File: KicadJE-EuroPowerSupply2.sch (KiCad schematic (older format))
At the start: 48 parts, among them J101 Laptop Power, J102 +-15V thru, J103 +-12v out, J104 +5V out, J105 Laptop Power Out, J106 FrontInterConnVin, J107 BaseInterConnVin, J108 FrontInterConnVout, J109 BaseInterConnVout, P101 Doepfer_Power_10pin, P102 Doepfer_Power_16pin, P105 Doepfer_Power_10pin, P106 Doepfer_Power_16pin, SW101 SW_SPDT

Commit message: Init 750mA indicator
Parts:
- removed J108: FrontInterConnVout, AJ-Dropbox-Kicad:BoardConnector2x2.54x10mm4pin, symbol Connector:Conn_01x04_Male
- removed J109: BaseInterConnVout, AJ-Dropbox-Kicad:BoardConnector2x2.54x10mm4pin, symbol Connector:Conn_01x04_Male
- removed TP101, TP107: RED Sleeve, TestPoint:TestPoint_THTPad_D2.0mm_Drill1.0mm, symbol Connector:TestPoint
- removed TP102, TP108: RED Banana, MountingHole:MountingHole_6.4mm_M6_ISO14580_Pad, symbol Connector:TestPoint
- removed TP103: BLUE Sleeve, TestPoint:TestPoint_THTPad_D2.0mm_Drill1.0mm, symbol Connector:TestPoint
- removed TP104: BLUE Banana, MountingHole:MountingHole_6.4mm_M6_ISO14580_Pad, symbol Connector:TestPoint
- removed TP105: BLACK Sleeve, TestPoint:TestPoint_THTPad_D2.0mm_Drill1.0mm, symbol Connector:TestPoint
- removed TP106: BLACK Banana, MountingHole:MountingHole_6.4mm_M6_ISO14580_Pad, symbol Connector:TestPoint
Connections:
- wire segments 233 -> 213
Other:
- moved on the sheet: J106, J107

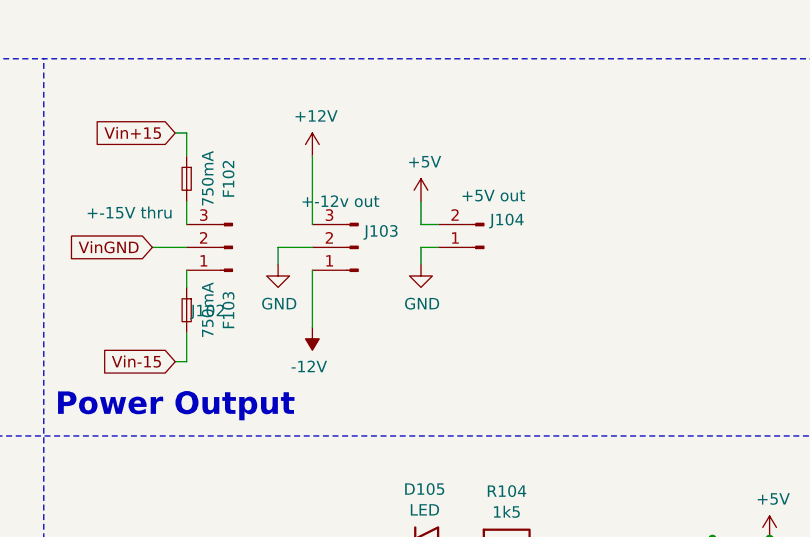
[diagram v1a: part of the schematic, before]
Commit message: placing first components
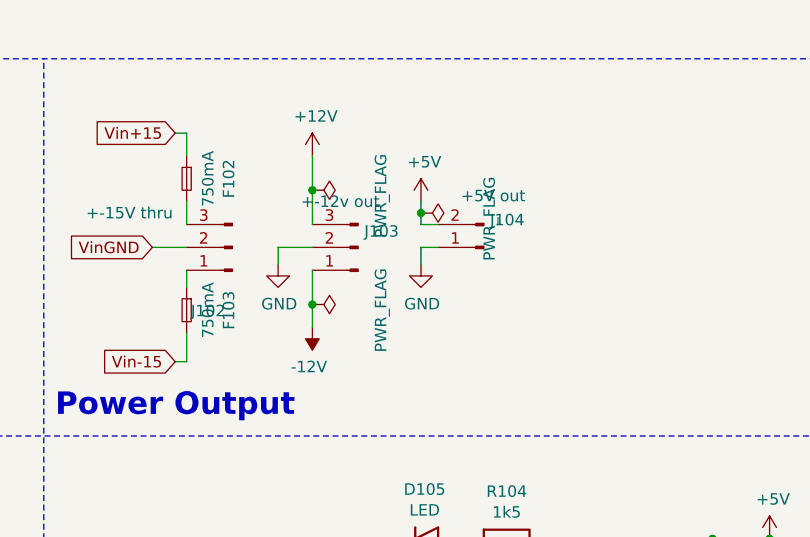
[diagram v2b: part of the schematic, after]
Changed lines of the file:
@@
 	5250 1800 5250 1925
 Wire Wire Line
-	5800 1025 5800 1325
-Wire Wire Line
-	5800 1775 5800 1525
+	5800 1025 5800 1175
+Wire Wire Line
+	5800 1775 5800 1675
 Wire Wire Line
 	4250 2625 4250 2825
@@
 	6350 1325 6275 1325
 Wire Wire Line
-	6275 1325 6275 1225
+	6275 1325 6275 1275
 $Comp
 L power:PWR_FLAG #FLG0101
@@
 Wire Notes Line
 	8350 3800 6000 3800
+$Comp
+L power:PWR_FLAG #FLG0104
+U 1 1 5F317544
+P 5800 1175
+AR Path="/5F317544" Ref="#FLG0104"  Part="1"
+AR Path="/5CBAA806/5F317544" Ref="#FLG?"  Part="1"
+F 0 "#FLG0104" H 5800 1250 50  0001 C CNN
+F 1 "PWR_FLAG" H 5825 1475 50  0000 C CNN
+F 2 "" H 5800 1175 50  0001 C CNN
+F 3 "~" H 5800 1175 50  0001 C CNN
+	1    5800 1175
+	0    1    1    0
+$EndComp
+Connection ~ 5800 1175
+Wire Wire Line
+	5800 1175 5800 1325
+$Comp
+L power:PWR_FLAG #FLG0105
+U 1 1 5F31A053
+P 5800 1675
+AR Path="/5F31A053" Ref="#FLG0105"  Part="1"
+AR Path="/5CBAA806/5F31A053" Ref="#FLG?"  Part="1"
+F 0 "#FLG0105" H 5800 1750 50  0001 C CNN
+F 1 "PWR_FLAG" H 5825 1975 50  0000 C CNN
+F 2 "" H 5800 1675 50  0001 C CNN
+F 3 "~" H 5800 1675 50  0001 C CNN
+	1    5800 1675
+	0    1    1    0
+$EndComp
+Connection ~ 5800 1675
+Wire Wire Line
+	5800 1675 5800 1525
+$Comp
+L power:PWR_FLAG #FLG0106
+U 1 1 5F31A50C
+P 6275 1275
+AR Path="/5F31A50C" Ref="#FLG0106"  Part="1"
+AR Path="/5CBAA806/5F31A50C" Ref="#FLG?"  Part="1"
+F 0 "#FLG0106" H 6275 1350 50  0001 C CNN
+F 1 "PWR_FLAG" H 6300 1575 50  0000 C CNN
+F 2 "" H 6275 1275 50  0001 C CNN
+F 3 "~" H 6275 1275 50  0001 C CNN
+	1    6275 1275
+	0    1    1    0
+$EndComp
+Connection ~ 6275 1275
+Wire Wire Line
+	6275 1275 6275 1225
 $EndSCHEMATC

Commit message: interboard connector
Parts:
- removed J107: BaseInterConnVin, AJ-Dropbox-Kicad:BoardConnector2x2.54x10mm4pin, symbol Connector:Conn_01x02_Male
- added J?: FrontInterConnVin, Connector_PinHeader_2.54mm:PinHeader_1x04_P2.54mm_Vertical, symbol Connector:Conn_01x04_Male
- added J? (x2): Conn_01x08, Connector_PinHeader_2.54mm:PinHeader_1x08_P2.54mm_Vertical, symbol Connector_Generic:Conn_01x08
- J106: footprint AJ-Dropbox-Kicad:BoardConnector2x2.54x10mm4pin -> Connector_PinHeader_2.54mm:PinHeader_1x04_P2.54mm_Vertical; symbol Connector:Conn_01x02_Male -> Connector:Conn_01x04_Male
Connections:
- net +12V: now also J?.5 (Pin_5), J?.5 (Pin_5)
- net +5V: now also J?.3 (Pin_3), J?.3 (Pin_3)
- net -12V: now also J?.7 (Pin_7), J?.7 (Pin_7)
- net GND: now also J?.1 (Pin_1), J?.1 (Pin_1), J?.8 (Pin_8), J?.8 (Pin_8)
- net Vin-Neg19: now also J106.3 (Pin_3), J106.4 (Pin_4), J?.3 (Pin_3), J?.4 (Pin_4); no longer J106.2 (Pin_2)
- net Vin-Pos19: now also J106.2 (Pin_2), J?.1 (Pin_1), J?.2 (Pin_2)
- new net I+12: J?.4 (Pin_4), J?.4 (Pin_4)
- new net I+5: J?.2 (Pin_2), J?.2 (Pin_2)
- new net I-12: J?.6 (Pin_6), J?.6 (Pin_6)
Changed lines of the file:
@@
 	6150 2900 7550 2900
 $Comp
-L Connector:Conn_01x02_Male J106
+L Connector:Conn_01x04_Male J106
 U 1 1 5C9B2CF1
 P 6275 4275
 F 0 "J106" H 6381 4453 50  0000 C CNN
 F 1 "FrontInterConnVin" H 6381 4362 50  0000 C CNN
-F 2 "AJ-Dropbox-Kicad:BoardConnector2x2.54x10mm4pin" H 6275 4275 50  0001 C CNN
+F 2 "Connector_PinHeader_2.54mm:PinHeader_1x04_P2.54mm_Vertical" H 6275 4275 50  0001 C CNN
 F 3 "~" H 6275 4275 50  0001 C CNN
 	1    6275 4275
 	1    0    0    -1
-$EndComp
-$Comp
-L Connector:Conn_01x02_Male J107
-U 1 1 5C9B2E76
-P 7425 4275
-F 0 "J107" H 7398 4248 50  0000 R CNN
-F 1 "BaseInterConnVin" H 7398 4157 50  0000 R CNN
-F 2 "AJ-Dropbox-Kicad:BoardConnector2x2.54x10mm4pin" H 7425 4275 50  0001 C CNN
-F 3 "~" H 7425 4275 50  0001 C CNN
-	1    7425 4275
-	-1   0    0    -1
 $EndComp
 Text GLabel 6975 4175 2    50   Input ~ 0
@@
 	6475 4375 6825 4375
 Wire Wire Line
-	7225 4275 6825 4275
-Wire Wire Line
 	6975 4475 6825 4475
 Wire Wire Line
 	6825 4475 6825 4375
 Connection ~ 6825 4375
-Wire Wire Line
-	6825 4375 7225 4375
 Wire Wire Line
 	6975 4175 6825 4175
@@
 Wire Wire Line
 	6275 1275 6275 1225
+Text GLabel 9150 4175 0    59   Input ~ 0
+I+5
+Wire Wire Line
+	9150 4175 9175 4175
+Text GLabel 9175 4575 0    59   Input ~ 0
+I-12
+Text GLabel 9175 4375 0    59   Input ~ 0
+I+12
+$Comp
+L Connector:Conn_01x04_Male J?
+U 1 1 5F5803FF
+P 7850 4275
+F 0 "J?" H 7956 4453 50  0000 C CNN
+F 1 "FrontInterConnVin" H 7956 4362 50  0000 C CNN
+F 2 "Connector_PinHeader_2.54mm:PinHeader_1x04_P2.54mm_Vertical" H 7850 4275 50  0001 C CNN
+F 3 "~" H 7850 4275 50  0001 C CNN
+	1    7850 4275
+	-1   0    0    -1
+$EndComp
+Wire Wire Line
+	7650 4175 7650 4275
+Wire Wire Line
+	6825 4275 7650 4275
+Connection ~ 7650 4275
+Wire Wire Line
+	7650 4475 7650 4375
+Wire Wire Line
+	6825 4375 7650 4375
+Connection ~ 7650 4375
+Wire Wire Line
+	6475 4475 6475 4375
+Connection ~ 6475 4375
+Wire Wire Line
+	6475 4275 6475 4175
+Connection ~ 6475 4275
+$Comp
+L power:-12V #PWR?
+U 1 1 5F5B2912
+P 9175 4675
+F 0 "#PWR?" H 9175 4775 50  0001 C CNN
+F 1 "-12V" H 9190 4848 50  0000 C CNN
+F 2 "" H 9175 4675 50  0001 C CNN
+F 3 "" H 9175 4675 50  0001 C CNN
+	1    9175 4675
+	0    -1   -1   0
+$EndComp
+$Comp
+L power:GND #PWR?
+U 1 1 5F5B2F3A
+P 9175 4775
+F 0 "#PWR?" H 9175 4525 50  0001 C CNN
+F 1 "GND" H 9180 4602 50  0000 C CNN
+F 2 "" H 9175 4775 50  0001 C CNN
+F 3 "" H 9175 4775 50  0001 C CNN
+	1    9175 4775
+	1    0    0    -1
+$EndComp
+$Comp
+L power:+12V #PWR?
+U 1 1 5F5B34B6
+P 9175 4475
+F 0 "#PWR?" H 9175 4325 50  0001 C CNN
+F 1 "+12V" H 9190 4648 50  0000 C CNN
+F 2 "" H 9175 4475 50  0001 C CNN
+F 3 "" H 9175 4475 50  0001 C CNN
+	1    9175 4475
+	0    -1   -1   0
+$EndComp
+$Comp
+L power:+5V #PWR?
+U 1 1 5F5B3CB4
+P 9175 4275
+F 0 "#PWR?" H 9175 4125 50  0001 C CNN
+F 1 "+5V" H 9190 4448 50  0000 C CNN
+F 2 "" H 9175 4275 50  0001 C CNN
+F 3 "" H 9175 4275 50  0001 C CNN
+	1    9175 4275
+	0    -1   -1   0
+$EndComp
+$Comp
+L Connector_Generic:Conn_01x08 J?
+U 1 1 5F5B43D9
+P 9375 4375
+F 0 "J?" H 9455 4367 50  0000 L CNN
+F 1 "Conn_01x08" H 9455 4276 50  0000 L CNN
+F 2 "Connector_PinHeader_2.54mm:PinHeader_1x08_P2.54mm_Vertical" H 9375 4375 50  0001 C CNN
+F 3 "~" H 9375 4375 50  0001 C CNN
+	1    9375 4375
+	1    0    0    -1
+$EndComp
+Wire Wire Line
+	9175 4775 8825 4775
+Wire Wire Line
+	8825 4775 8825 4075
+Wire Wire Line
+	8825 4075 9175 4075
+Connection ~ 9175 4775
+Text GLabel 10325 4175 0    59   Input ~ 0
+I+5
+Wire Wire Line
+	10325 4175 10350 4175
+Text GLabel 10350 4575 0    59   Input ~ 0
+I-12
+Text GLabel 10350 4375 0    59   Input ~ 0
+I+12
+$Comp
+L power:-12V #PWR?
+U 1 1 5F62ABF4
+P 10350 4675
+F 0 "#PWR?" H 10350 4775 50  0001 C CNN
+F 1 "-12V" H 10365 4848 50  0000 C CNN
+F 2 "" H 10350 4675 50  0001 C CNN
+F 3 "" H 10350 4675 50  0001 C CNN
+	1    10350 4675
+	0    -1   -1   0
+$EndComp
+$Comp
+L power:GND #PWR?
+U 1 1 5F62ABFE
+P 10350 4775
+F 0 "#PWR?" H 10350 4525 50  0001 C CNN
+F 1 "GND" H 10355 4602 50  0000 C CNN
+F 2 "" H 10350 4775 50  0001 C CNN
+F 3 "" H 10350 4775 50  0001 C CNN
+	1    10350 4775
+	1    0    0    -1
+$EndComp
+$Comp
+L power:+12V #PWR?
+U 1 1 5F62AC08
+P 10350 4475
+F 0 "#PWR?" H 10350 4325 50  0001 C CNN
+F 1 "+12V" H 10365 4648 50  0000 C CNN
+F 2 "" H 10350 4475 50  0001 C CNN
+F 3 "" H 10350 4475 50  0001 C CNN
+	1    10350 4475
+	0    -1   -1   0
+$EndComp
+$Comp
+L power:+5V #PWR?
+U 1 1 5F62AC12
+P 10350 4275
+F 0 "#PWR?" H 10350 4125 50  0001 C CNN
+F 1 "+5V" H 10365 4448 50  0000 C CNN
+F 2 "" H 10350 4275 50  0001 C CNN
+F 3 "" H 10350 4275 50  0001 C CNN
+	1    10350 4275
+	0    -1   -1   0
+$EndComp
+$Comp
+L Connector_Generic:Conn_01x08 J?
+U 1 1 5F62AC1C
+P 10550 4375
+F 0 "J?" H 10630 4367 50  0000 L CNN
+F 1 "Conn_01x08" H 10630 4276 50  0000 L CNN
+F 2 "Connector_PinHeader_2.54mm:PinHeader_1x08_P2.54mm_Vertical" H 10550 4375 50  0001 C CNN
+F 3 "~" H 10550 4375 50  0001 C CNN
+	1    10550 4375
+	1    0    0    -1
+$EndComp
+Wire Wire Line
+	10350 4775 10000 4775
+Wire Wire Line
+	10000 4775 10000 4075
+Wire Wire Line
+	10000 4075 10350 4075
+Connection ~ 10350 4775
 $EndSCHEMATC

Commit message: Almost completely placed
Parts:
- gave numbers to parts that had none: 3
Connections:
- net +12V: now also J108.3 (Pin_3), J109.3 (Pin_3); no longer J108.5 (Pin_5), J109.5 (Pin_5)
- net +5V: now also J108.5 (Pin_5), J109.5 (Pin_5); no longer J108.3 (Pin_3), J109.3 (Pin_3)
- net I+12: now also J108.2 (Pin_2), J109.2 (Pin_2); no longer J108.4 (Pin_4), J109.4 (Pin_4)
- net I+5: now also J108.4 (Pin_4), J109.4 (Pin_4); no longer J108.2 (Pin_2), J109.2 (Pin_2)
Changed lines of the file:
@@
 Wire Wire Line
 	6275 1275 6275 1225
-Text GLabel 9150 4175 0    59   Input ~ 0
+Text GLabel 9175 4375 0    59   Input ~ 0
 I+5
-Wire Wire Line
-	9150 4175 9175 4175
 Text GLabel 9175 4575 0    59   Input ~ 0
 I-12
-Text GLabel 9175 4375 0    59   Input ~ 0
+Text GLabel 9175 4175 0    59   Input ~ 0
 I+12
 $Comp
-L Connector:Conn_01x04_Male J?
+L Connector:Conn_01x04_Male J107
 U 1 1 5F5803FF
 P 7850 4275
-F 0 "J?" H 7956 4453 50  0000 C CNN
+F 0 "J107" H 7956 4453 50  0000 C CNN
 F 1 "FrontInterConnVin" H 7956 4362 50  0000 C CNN
 F 2 "Connector_PinHeader_2.54mm:PinHeader_1x04_P2.54mm_Vertical" H 7850 4275 50  0001 C CNN
@@
 Connection ~ 6475 4275
 $Comp
-L power:-12V #PWR?
+L power:-12V #PWR0101
 U 1 1 5F5B2912
 P 9175 4675
-F 0 "#PWR?" H 9175 4775 50  0001 C CNN
+F 0 "#PWR0101" H 9175 4775 50  0001 C CNN
 F 1 "-12V" H 9190 4848 50  0000 C CNN
 F 2 "" H 9175 4675 50  0001 C CNN
@@
 $EndComp
 $Comp
-L power:GND #PWR?
+L power:GND #PWR0102
 U 1 1 5F5B2F3A
 P 9175 4775
-F 0 "#PWR?" H 9175 4525 50  0001 C CNN
+F 0 "#PWR0102" H 9175 4525 50  0001 C CNN
 F 1 "GND" H 9180 4602 50  0000 C CNN
 F 2 "" H 9175 4775 50  0001 C CNN
@@
 $EndComp
 $Comp
-L power:+12V #PWR?
+L power:+12V #PWR0103
 U 1 1 5F5B34B6
+P 9175 4275
+F 0 "#PWR0103" H 9175 4125 50  0001 C CNN
+F 1 "+12V" H 9190 4448 50  0000 C CNN
+F 2 "" H 9175 4275 50  0001 C CNN
+F 3 "" H 9175 4275 50  0001 C CNN
+	1    9175 4275
+	0    -1   -1   0
+$EndComp
+$Comp
+L power:+5V #PWR0104
+U 1 1 5F5B3CB4
 P 9175 4475
-F 0 "#PWR?" H 9175 4325 50  0001 C CNN
-F 1 "+12V" H 9190 4648 50  0000 C CNN
+F 0 "#PWR0104" H 9175 4325 50  0001 C CNN
+F 1 "+5V" H 9190 4648 50  0000 C CNN
 F 2 "" H 9175 4475 50  0001 C CNN
 F 3 "" H 9175 4475 50  0001 C CNN
@@
 $EndComp
 $Comp
-L power:+5V #PWR?
-U 1 1 5F5B3CB4
-P 9175 4275
-F 0 "#PWR?" H 9175 4125 50  0001 C CNN
-F 1 "+5V" H 9190 4448 50  0000 C CNN
-F 2 "" H 9175 4275 50  0001 C CNN
-F 3 "" H 9175 4275 50  0001 C CNN
-	1    9175 4275
-	0    -1   -1   0
-$EndComp
-$Comp
-L Connector_Generic:Conn_01x08 J?
+L Connector_Generic:Conn_01x08 J108
 U 1 1 5F5B43D9
 P 9375 4375
-F 0 "J?" H 9455 4367 50  0000 L CNN
+F 0 "J108" H 9455 4367 50  0000 L CNN
 F 1 "Conn_01x08" H 9455 4276 50  0000 L CNN
 F 2 "Connector_PinHeader_2.54mm:PinHeader_1x08_P2.54mm_Vertical" H 9375 4375 50  0001 C CNN
@@
 	8825 4075 9175 4075
 Connection ~ 9175 4775
-Text GLabel 10325 4175 0    59   Input ~ 0
+Text GLabel 10350 4375 0    59   Input ~ 0
 I+5
-Wire Wire Line
-	10325 4175 10350 4175
 Text GLabel 10350 4575 0    59   Input ~ 0
 I-12
-Text GLabel 10350 4375 0    59   Input ~ 0
+Text GLabel 10350 4175 0    59   Input ~ 0
 I+12
 $Comp
-L power:-12V #PWR?
+L power:-12V #PWR0116
 U 1 1 5F62ABF4
 P 10350 4675
-F 0 "#PWR?" H 10350 4775 50  0001 C CNN
+F 0 "#PWR0116" H 10350 4775 50  0001 C CNN
 F 1 "-12V" H 10365 4848 50  0000 C CNN
 F 2 "" H 10350 4675 50  0001 C CNN
@@
 $EndComp
 $Comp
-L power:GND #PWR?
+L power:GND #PWR0120
 U 1 1 5F62ABFE
 P 10350 4775
-F 0 "#PWR?" H 10350 4525 50  0001 C CNN
+F 0 "#PWR0120" H 10350 4525 50  0001 C CNN
 F 1 "GND" H 10355 4602 50  0000 C CNN
 F 2 "" H 10350 4775 50  0001 C CNN
@@
 $EndComp
 $Comp
-L power:+12V #PWR?
+L power:+12V #PWR0122
 U 1 1 5F62AC08
+P 10350 4275
+F 0 "#PWR0122" H 10350 4125 50  0001 C CNN
+F 1 "+12V" H 10365 4448 50  0000 C CNN
+F 2 "" H 10350 4275 50  0001 C CNN
+F 3 "" H 10350 4275 50  0001 C CNN
+	1    10350 4275
+	0    -1   -1   0
+$EndComp
+$Comp
+L power:+5V #PWR0124
+U 1 1 5F62AC12
 P 10350 4475
-F 0 "#PWR?" H 10350 4325 50  0001 C CNN
-F 1 "+12V" H 10365 4648 50  0000 C CNN
+F 0 "#PWR0124" H 10350 4325 50  0001 C CNN
+F 1 "+5V" H 10365 4648 50  0000 C CNN
 F 2 "" H 10350 4475 50  0001 C CNN
 F 3 "" H 10350 4475 50  0001 C CNN
@@
 $EndComp
 $Comp
-L power:+5V #PWR?
-U 1 1 5F62AC12
-P 10350 4275
-F 0 "#PWR?" H 10350 4125 50  0001 C CNN
-F 1 "+5V" H 10365 4448 50  0000 C CNN
-F 2 "" H 10350 4275 50  0001 C CNN
-F 3 "" H 10350 4275 50  0001 C CNN
-	1    10350 4275
-	0    -1   -1   0
-$EndComp
-$Comp
-L Connector_Generic:Conn_01x08 J?
+L Connector_Generic:Conn_01x08 J109
 U 1 1 5F62AC1C
 P 10550 4375
-F 0 "J?" H 10630 4367 50  0000 L CNN
+F 0 "J109" H 10630 4367 50  0000 L CNN
 F 1 "Conn_01x08" H 10630 4276 50  0000 L CNN
 F 2 "Connector_PinHeader_2.54mm:PinHeader_1x08_P2.54mm_Vertical" H 10550 4375 50  0001 C CNN
